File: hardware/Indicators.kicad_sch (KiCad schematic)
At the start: 39 parts, among them IC9 74LVC1G17GW,125, U2 74LVC594AD,118, U27 74LVC594AD,118

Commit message: updated kicad and started on gamer led
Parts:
- added D45: WS2812B-2020, LED_SMD:LED_WS2812B-2020_PLCC4_2.0x2.0mm, symbol LED:WS2812B-2020
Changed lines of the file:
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@@
+	)
+	(symbol
+		(lib_id "LED:WS2812B-2020")
+		(at 189.23 101.6 0)
+		(unit 1)
+		(exclude_from_sim no)
+		(in_bom yes)
+		(on_board yes)
+		(dnp no)
+		(fields_autoplaced yes)
+		(property "Reference" "D45"
+			(at 203.2 95.1798 0)
+			(effects
+				(font
+					(size 1.27 1.27)
+				)
+			)
+		)
+		(property "Value" "WS2812B-2020"
+			(at 203.2 97.7198 0)
+			(effects
+				(font
+					(size 1.27 1.27)
+				)
+			)
+		)
+		(property "Footprint" "LED_SMD:LED_WS2812B-2020_PLCC4_2.0x2.0mm"
+			(at 190.5 109.22 0)
+			(effects
+				(font
+					(size 1.27 1.27)
+				)
+				(justify left top)
+				(hide yes)
+			)
+		)
+		(property "Datasheet" "https://cdn-shop.adafruit.com/product-files/4684/4684_WS2812B-2020_V1.3_EN.pdf"
+			(at 191.77 111.125 0)
+			(effects
+				(font
+					(size 1.27 1.27)
+				)
+				(justify left top)
+				(hide yes)
+			)
+		)
+		(property "Description" "RGB LED with integrated controller, 2.0 x 2.0 mm, 12 mA"
+			(at 189.23 101.6 0)
+			(effects
+				(font
+					(size 1.27 1.27)
+				)
+				(hide yes)
+			)
+		)
+		(pin "3"
+		)
+		(pin "4"
+		)
+		(pin "2"
+		)
+		(pin "1"
+		)
+		(instances
+			(project ""
+				(path "/eb16378f-e371-46a9-bfab-b0d9404d0362/9558d30f-15cc-469d-b921-6b74808d7dd0"
+					(reference "D45")
+					(unit 1)
+				)
+			)
+		)
 	)
 	(symbol

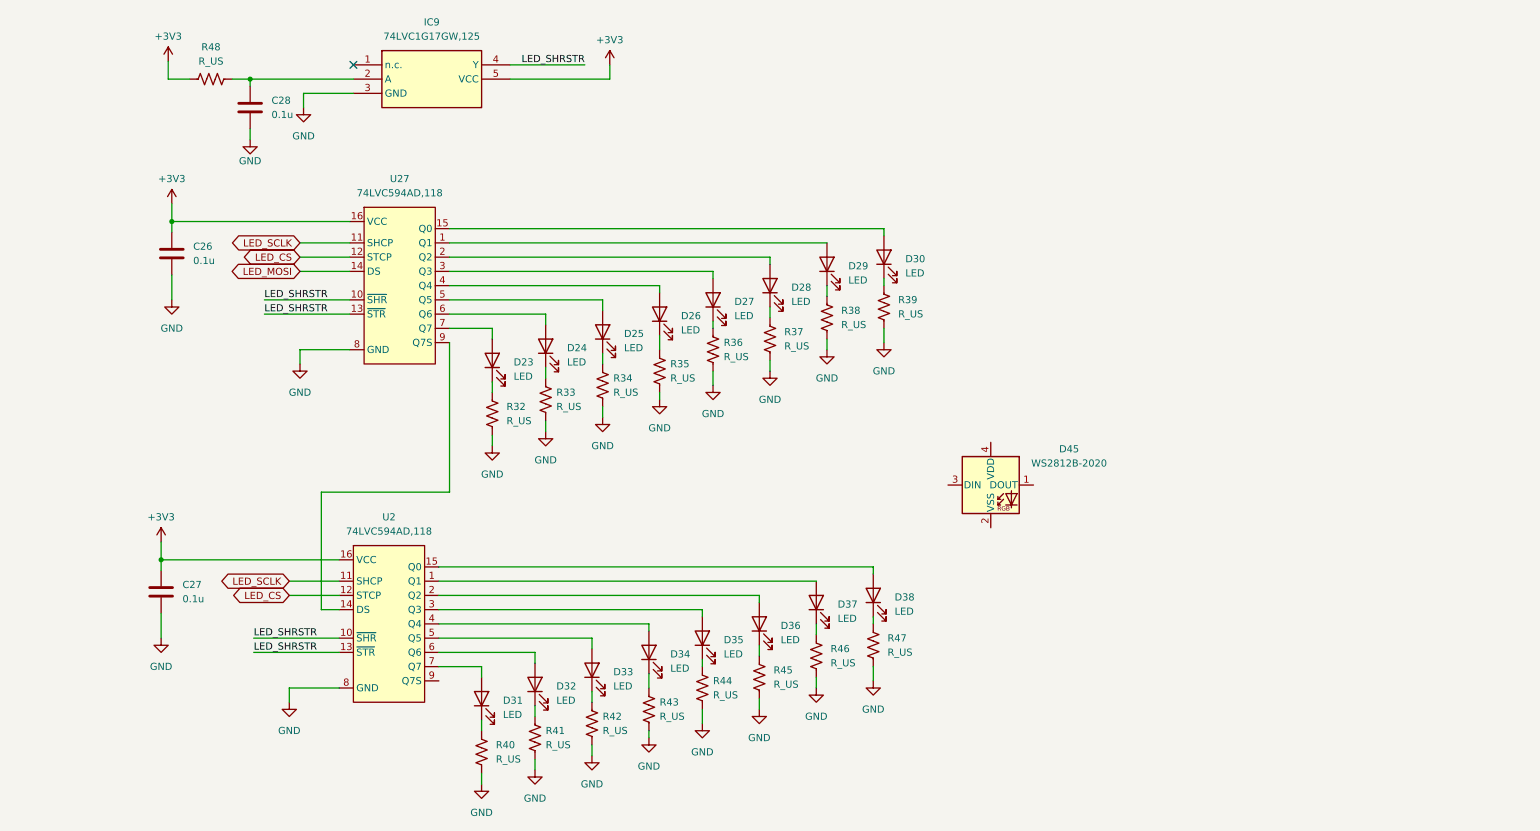
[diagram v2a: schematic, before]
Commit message: added gamer led but need to make pretty
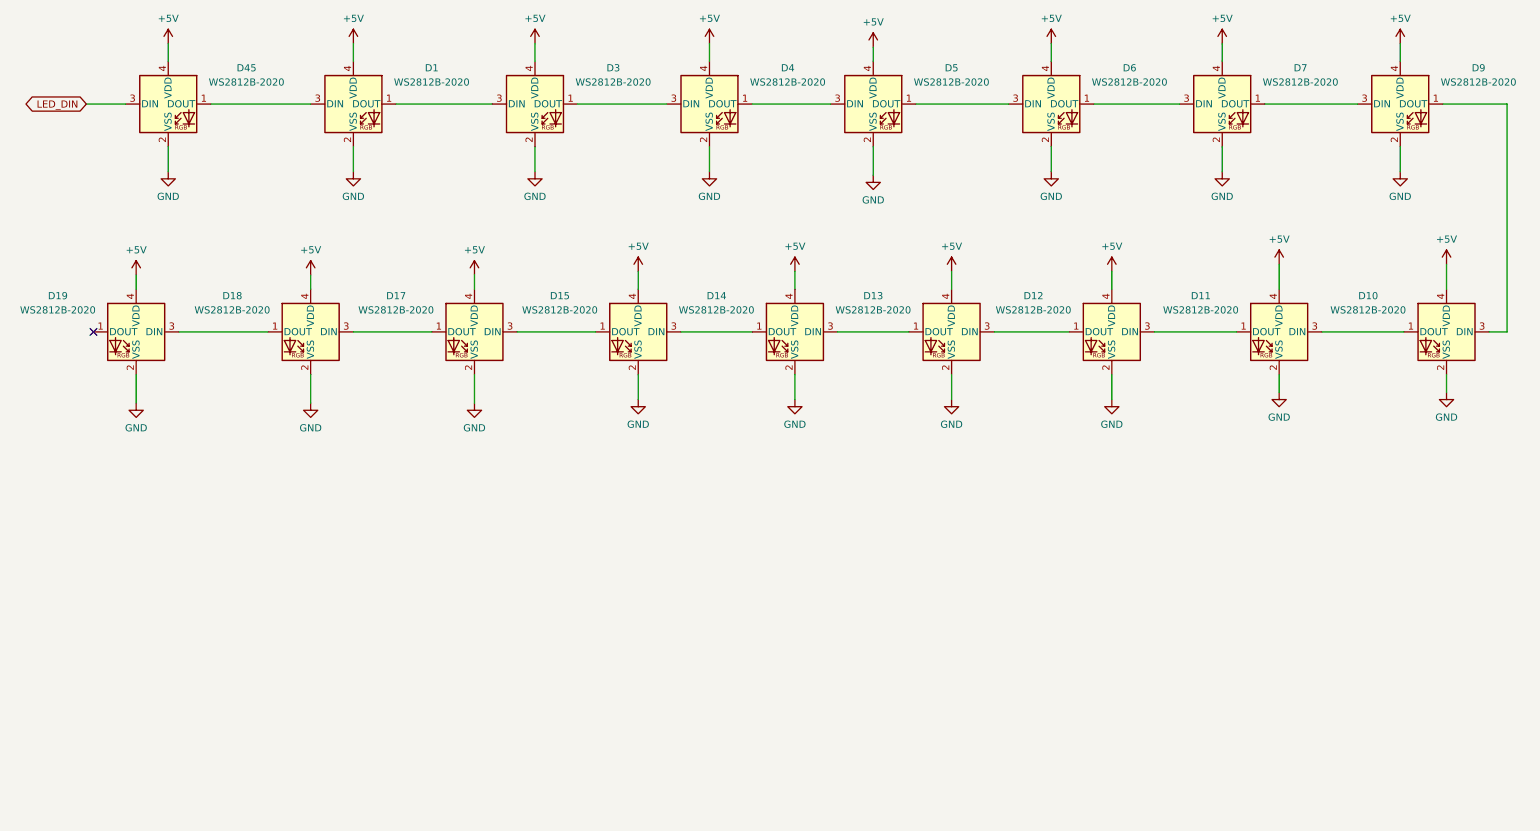
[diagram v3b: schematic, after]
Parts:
- removed C26, C27, C28: 0.1u, symbol Device:C
- removed D23, D24, D25, D26, D27, D28, D29, D30, D31, D32, D33, D34, D35, D36, D37, D38: LED, symbol Device:LED
- removed IC9: 74LVC1G17GW,125, SOT65P212X110-5N, symbol PDU_74LVC1G17GW,125:74LVC1G17GW,125
- removed R32, R33, R34, R35, R36, R37, R38, R39, R40, R41, R42, R43, R44, R45, R46, R47, R48: R_US, symbol Device:R_US
- removed U2, U27: 74LVC594AD,118, Package_SO:SOIC-16_3.9x9.9mm_P1.27mm, symbol PowerDistributionUnitLib:74LVC594AD,118
- added D1, D10, D11, D12, D13, D14, D15, D17, D18, D19, D3, D4, D5, D6, D7, D9: WS2812B-2020, LED_SMD:LED_WS2812B-2020_PLCC4_2.0x2.0mm, symbol LED:WS2812B-2020
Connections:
- net GND: now also D45.2 (VSS), D1.2 (VSS), D10.2 (VSS), D11.2 (VSS), D12.2 (VSS), D13.2 (VSS), D14.2 (VSS), D15.2 (VSS), D17.2 (VSS), D18.2 (VSS), D19.2 (VSS), D3.2 (VSS), D4.2 (VSS), D5.2 (VSS), D6.2 (VSS), D7.2 (VSS), D9.2 (VSS)
- net at D45.1 (DOUT): now also D1.3 (DIN)
- net LED_DIN: now reaches D45.3 (DIN)
- net +5V: now reaches D45.4 (VDD)
- net +5V: now also D1.4 (VDD), D10.4 (VDD), D11.4 (VDD), D12.4 (VDD), D13.4 (VDD), D14.4 (VDD), D15.4 (VDD), D17.4 (VDD), D18.4 (VDD), D19.4 (VDD), D3.4 (VDD), D4.4 (VDD), D5.4 (VDD), D6.4 (VDD), D7.4 (VDD), D9.4 (VDD)
- new net: D10.1 (DOUT), D11.3 (DIN)
- new net: D10.3 (DIN), D9.1 (DOUT)
- new net: D3.1 (DOUT), D4.3 (DIN)
- new net: D1.1 (DOUT), D3.3 (DIN)
- new net: D6.1 (DOUT), D7.3 (DIN)
- new net: D5.1 (DOUT), D6.3 (DIN)
- new net: D7.1 (DOUT), D9.3 (DIN)
- new net: D14.1 (DOUT), D15.3 (DIN)
- new net: D13.1 (DOUT), D14.3 (DIN)
- new net: D15.1 (DOUT), D17.3 (DIN)
- new net: D4.1 (DOUT), D5.3 (DIN)
- new net: D18.1 (DOUT), D19.3 (DIN)
- new net: D12.1 (DOUT), D13.3 (DIN)
- new net: D11.1 (DOUT), D12.3 (DIN)
- new net: D17.1 (DOUT), D18.3 (DIN)
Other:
- moved on the sheet: D45

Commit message: discrete cs
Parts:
- renumbered D19 to D1, D5 to D10, D13 to D11, D6 to D12, D12 to D13, D7 to D14, D11 to D15, D9 to D16, D10 to D17, D45 to D2, D18 to D3, D1 to D4, D17 to D5, D3 to D6, D15 to D7, D4 to D8, D14 to D9

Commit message: surahbi comment mostly done except led
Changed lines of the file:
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@@
 		)
 	)
-	(global_label "LED_DIN"
-		(shape bidirectional)
+	(hierarchical_label "LED_DIN"
+		(shape input)
 		(at 27.94 33.655 180)
-		(fields_autoplaced yes)
 		(effects
 			(font
@@
 			(justify right)
 		)
-		(property "Intersheetrefs" "${INTERSHEET_REFS}"
-			(at 16.2235 33.655 0)
-			(hide yes)
-			(show_name no)
-			(do_not_autoplace no)
-			(effects
-				(font
-					(size 1.27 1.27)
-				)
-				(justify right)
-			)
-		)
 	)

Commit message: maybe added tvs
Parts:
- D38: renamed from D1; LCSC P/N (none) -> C965555
- D39: renamed from D2; LCSC P/N (none) -> C965555
- D40: renamed from D3; LCSC P/N (none) -> C965555
- D41: renamed from D4; LCSC P/N (none) -> C965555
- D42: renamed from D5; LCSC P/N (none) -> C965555
- D43: renamed from D6; LCSC P/N (none) -> C965555
- D44: renamed from D7; LCSC P/N (none) -> C965555
- D45: renamed from D8; LCSC P/N (none) -> C965555
- D46: renamed from D9; LCSC P/N (none) -> C965555
- D47: renamed from D10; LCSC P/N (none) -> C965555
- D48: renamed from D11; LCSC P/N (none) -> C965555
- D49: renamed from D12; LCSC P/N (none) -> C965555
- D50: renamed from D13; LCSC P/N (none) -> C965555
- D51: renamed from D14; LCSC P/N (none) -> C965555
- D52: renamed from D15; LCSC P/N (none) -> C965555
- D53: renamed from D16; LCSC P/N (none) -> C965555
- D54: renamed from D17; LCSC P/N (none) -> C965555
